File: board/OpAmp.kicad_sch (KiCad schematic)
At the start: 16 parts, among them U4 ${SIM.PARAMS}, U5 ${SIM.PARAMS}, U6 ${SIM.PARAMS}

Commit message: Add OpAmp link
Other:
- note added: "LM358DT"
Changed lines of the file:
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@@
 	(generator_version "9.0")
 	(paper "A4")
+	(text "LM358DT"
+		(exclude_from_sim no)
+		(at 69.088 146.558 0)
+		(effects
+			(font
+				(size 1.27 1.27)
+			)
+			(href "https://www.digikey.com/en/products/detail/stmicroelectronics/LM358DT/591693")
+		)
+	)
 	(junction
 		(at 172.72 133.35)

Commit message: fixed some review issues and footprints
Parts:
- Conn4: footprint (none) -> MRDT_Connectors:MOLEX_SL_04_Vertical
- R10, R11, R12, R13, R14, R15, R4, R5, R6, R7, R8, R9: footprint (none) -> Resistor_SMD:R_0603_1608Metric_Pad0.98x0.95mm_HandSolder
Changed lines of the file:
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@@
 			)
 		)
-		(property "Footprint" ""
+		(property "Footprint" "Resistor_SMD:R_0603_1608Metric_Pad0.98x0.95mm_HandSolder"
 			(at 171.704 139.446 90)
 			(effects
@@
 			)
 		)
-		(property "Footprint" ""
+		(property "Footprint" "Resistor_SMD:R_0603_1608Metric_Pad0.98x0.95mm_HandSolder"
 			(at 122.174 138.176 90)
 			(effects
@@
 			)
 		)
-		(property "Footprint" ""
+		(property "Footprint" "Resistor_SMD:R_0603_1608Metric_Pad0.98x0.95mm_HandSolder"
 			(at 138.684 131.064 90)
 			(effects
@@
 			)
 		)
-		(property "Footprint" ""
+		(property "Footprint" "Resistor_SMD:R_0603_1608Metric_Pad0.98x0.95mm_HandSolder"
 			(at 127.254 138.176 90)
 			(effects
@@
 			)
 		)
-		(property "Footprint" ""
+		(property "Footprint" "Resistor_SMD:R_0603_1608Metric_Pad0.98x0.95mm_HandSolder"
 			(at 225.044 139.446 90)
 			(effects
@@
 			)
 		)
-		(property "Footprint" ""
+		(property "Footprint" "Resistor_SMD:R_0603_1608Metric_Pad0.98x0.95mm_HandSolder"
 			(at 236.474 132.334 90)
 			(effects
@@
 			)
 		)
-		(property "Footprint" ""
+		(property "Footprint" "Resistor_SMD:R_0603_1608Metric_Pad0.98x0.95mm_HandSolder"
 			(at 108.204 117.856 90)
 			(effects
@@
 			)
 		)
-		(property "Footprint" ""
+		(property "Footprint" "Resistor_SMD:R_0603_1608Metric_Pad0.98x0.95mm_HandSolder"
 			(at 176.784 139.446 90)
 			(effects
@@
 			)
 		)
-		(property "Footprint" ""
+		(property "Footprint" "Resistor_SMD:R_0603_1608Metric_Pad0.98x0.95mm_HandSolder"
 			(at 219.964 139.446 90)
 			(effects
@@
 			)
 		)
-		(property "Footprint" ""
+		(property "Footprint" "Resistor_SMD:R_0603_1608Metric_Pad0.98x0.95mm_HandSolder"
 			(at 205.994 119.126 90)
 			(effects
@@
 			)
 		)
-		(property "Footprint" ""
+		(property "Footprint" "MRDT_Connectors:MOLEX_SL_04_Vertical"
 			(at 247.65 76.2 0)
 			(effects
@@
 			)
 		)
-		(property "Footprint" ""
+		(property "Footprint" "Resistor_SMD:R_0603_1608Metric_Pad0.98x0.95mm_HandSolder"
 			(at 157.734 119.126 90)
 			(effects
@@
 			)
 		)
-		(property "Footprint" ""
+		(property "Footprint" "Resistor_SMD:R_0603_1608Metric_Pad0.98x0.95mm_HandSolder"
 			(at 188.214 132.334 90)
 			(effects

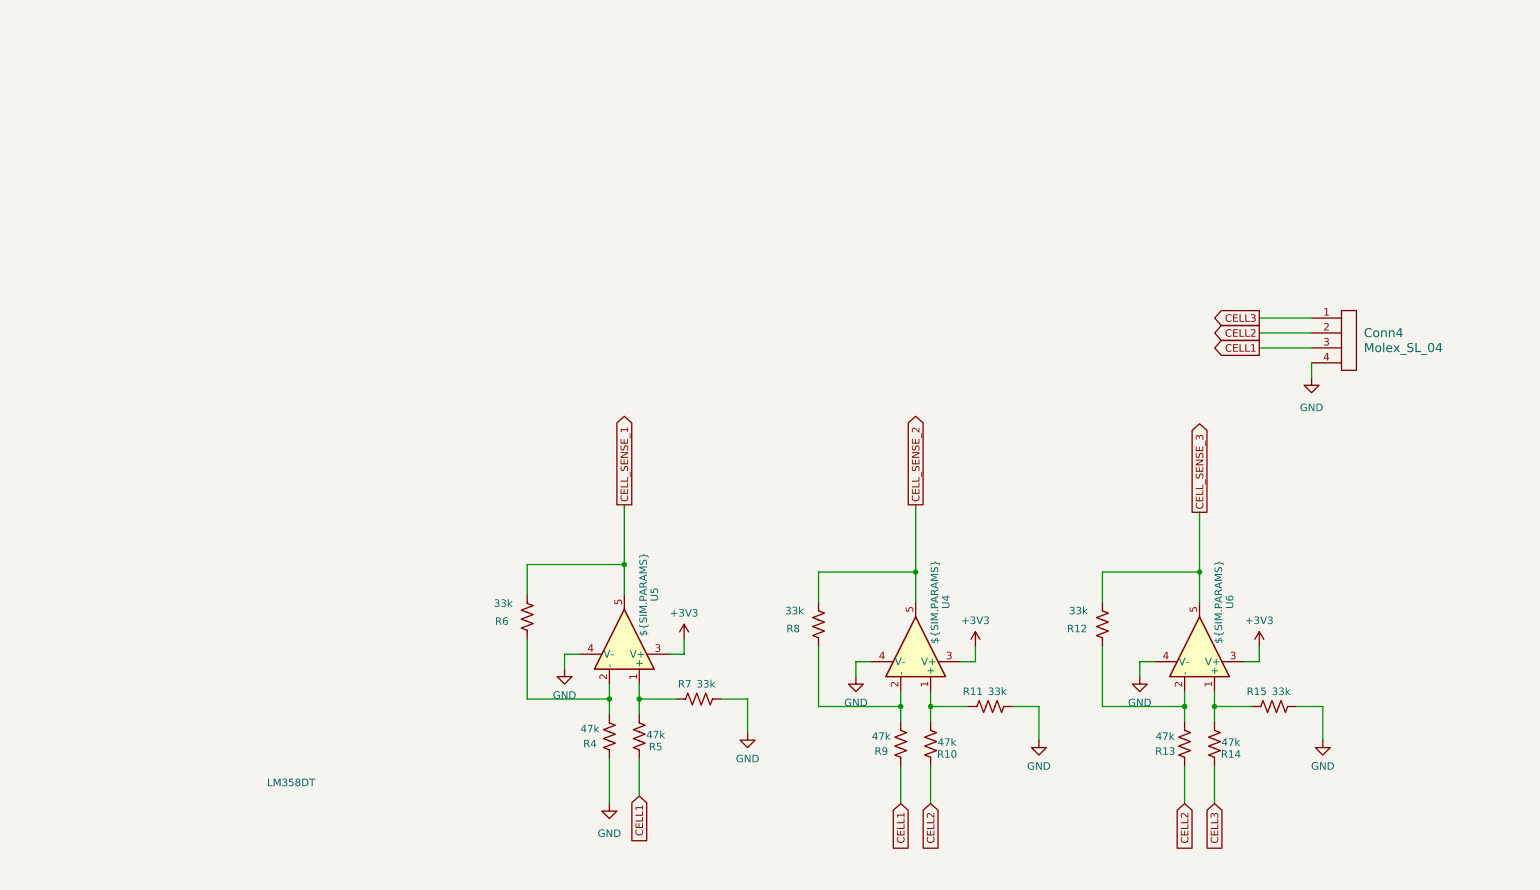
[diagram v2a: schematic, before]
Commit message: Change Gate Driver and Op amp
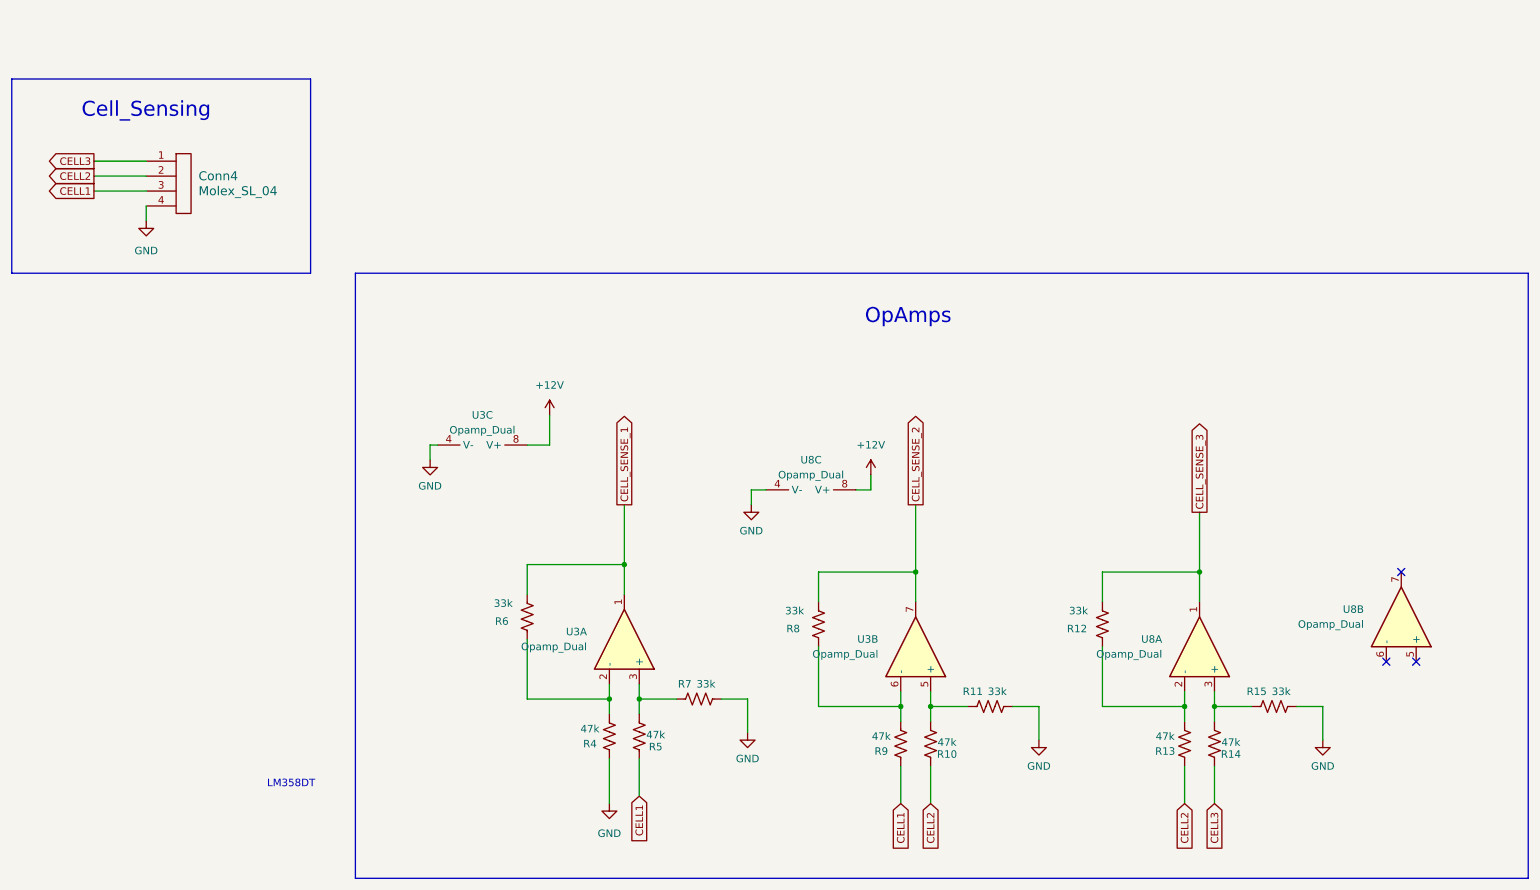
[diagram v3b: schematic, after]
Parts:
- removed U4, U5, U6: ${SIM.PARAMS}, symbol Simulation_SPICE:OPAMP
- added U3, U8: Opamp_Dual, symbol Device:Opamp_Dual
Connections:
- net CELL_SENSE_1: now also U3.1
- net CELL_SENSE_2: now also U3.7
- net CELL_SENSE_3: now also U8.1
- net GND: now also U3.4 (V-), U8.4 (V-)
- net at R8.1, R9.2: now also U3.6 (-)
- net at R4.2, R6.1: now also U3.2 (-)
- net at R5.2, R7.1: now also U3.3 (+)
- net at R14.2, R15.1: now also U8.3 (+)
- net at R10.2, R11.1: now also U3.5 (+)
- net at R12.1, R13.2: now also U8.2 (-)
- new net +12V: U3.8 (V+), U8.8 (V+)
- no-connect marks 0 -> 3
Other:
- note added: "Cell_Sensing"
- note added: "OpAmps"
- moved on the sheet: Conn4

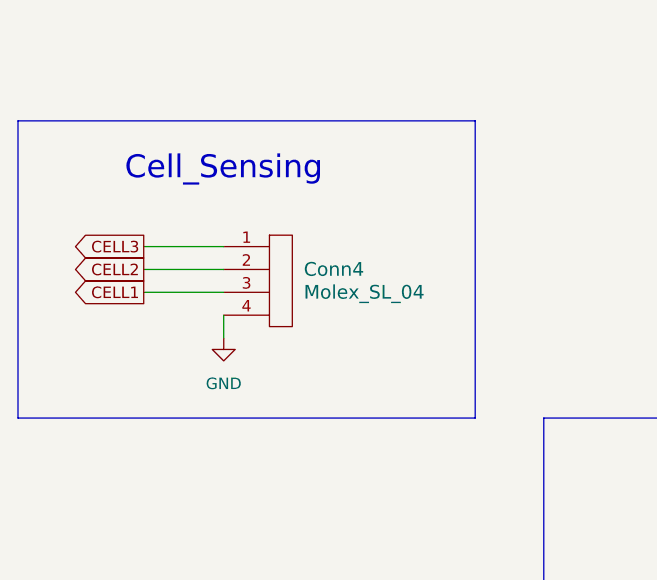
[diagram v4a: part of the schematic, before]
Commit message: fixed tags added buzzer
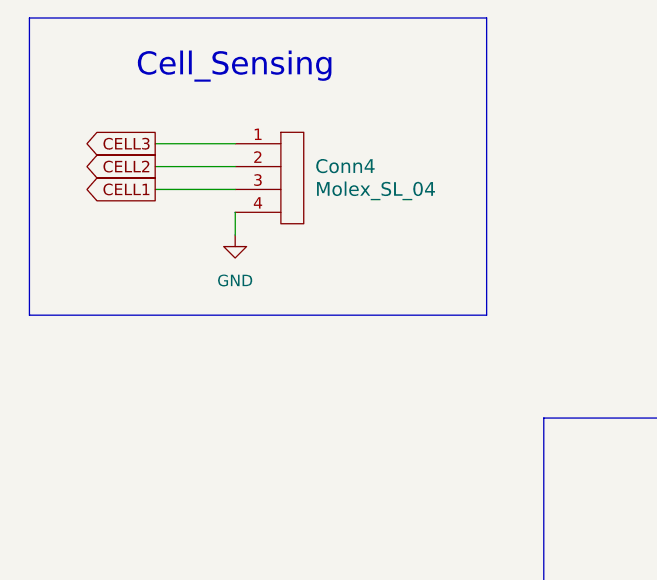
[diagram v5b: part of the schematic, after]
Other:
- moved on the sheet: Conn4
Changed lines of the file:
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@@
 	(paper "A4")
 	(rectangle
-		(start 21.59 26.67)
-		(end 72.39 59.69)
+		(start 22.86 15.24)
+		(end 73.66 48.26)
 		(stroke
 			(width 0)
@@
 	(text "Cell_Sensing"
 		(exclude_from_sim no)
-		(at 44.45 32.004 0)
+		(at 45.72 20.574 0)
 		(effects
 			(font
@@
 	(wire
 		(pts
-			(xy 35.56 40.64) (xy 44.45 40.64)
-		)
-		(stroke
-			(width 0)
-			(type default)
-		)
-	)
-	(wire
-		(pts
-			(xy 35.56 43.18) (xy 44.45 43.18)
+			(xy 36.83 29.21) (xy 45.72 29.21)
+		)
+		(stroke
+			(width 0)
+			(type default)
+		)
+	)
+	(wire
+		(pts
+			(xy 36.83 31.75) (xy 45.72 31.75)
 		)
 		(stroke
@@
 	(wire
 		(pts
-			(xy 35.56 45.72) (xy 44.45 45.72)
+			(xy 36.83 34.29) (xy 45.72 34.29)
 		)
 		(stroke
@@
 	(wire
 		(pts
-			(xy 44.45 50.8) (xy 44.45 48.26)
+			(xy 45.72 39.37) (xy 45.72 36.83)
 		)
 		(stroke
@@
 	(global_label "CELL1"
 		(shape output)
-		(at 35.56 45.72 180)
+		(at 36.83 34.29 180)
 		(fields_autoplaced yes)
 		(effects
@@
 		)
 		(property "Intersheetrefs" "${INTERSHEET_REFS}"
-			(at 26.8901 45.72 0)
+			(at 28.1601 34.29 0)
 			(effects
 				(font
@@
 	(global_label "CELL3"
 		(shape output)
-		(at 35.56 40.64 180)
+		(at 36.83 29.21 180)
 		(fields_autoplaced yes)
 		(effects
@@
 		)
 		(property "Intersheetrefs" "${INTERSHEET_REFS}"
-			(at 26.8901 40.64 0)
+			(at 28.1601 29.21 0)
 			(effects
 				(font
@@
 	(global_label "CELL2"
 		(shape output)
-		(at 35.56 43.18 180)
+		(at 36.83 31.75 180)
 		(fields_autoplaced yes)
 		(effects
@@
 		)
 		(property "Intersheetrefs" "${INTERSHEET_REFS}"
-			(at 26.8901 43.18 0)
+			(at 28.1601 31.75 0)
 			(effects
 				(font
@@
 	(symbol
 		(lib_id "power:GND")
-		(at 44.45 50.8 0)
+		(at 45.72 39.37 0)
 		(unit 1)
 		(exclude_from_sim no)
@@
 		(fields_autoplaced yes)
 		(property "Reference" "#PWR021"
-			(at 44.45 57.15 0)
+			(at 45.72 45.72 0)
 			(effects
 				(font
@@
 		)
 		(property "Value" "GND"
-			(at 44.45 55.88 0)
+			(at 45.72 44.45 0)
 			(effects
 				(font
@@
 		)
 		(property "Footprint" ""
-			(at 44.45 50.8 0)
+			(at 45.72 39.37 0)
 			(effects
 				(font
@@
 		)
 		(property "Datasheet" ""
-			(at 44.45 50.8 0)
+			(at 45.72 39.37 0)
 			(effects
 				(font
@@
 		)
 		(property "Description" "Power symbol creates a global label with name \"GND\" , ground"
-			(at 44.45 50.8 0)
+			(at 45.72 39.37 0)
 			(effects
 				(font
@@
 	(symbol
 		(lib_id "MRDT_Connectors:Molex_SL_04")
-		(at 49.53 49.53 0)
+		(at 50.8 38.1 0)
 		(unit 1)
 		(exclude_from_sim no)
@@
 		(fields_autoplaced yes)
 		(property "Reference" "Conn4"
-			(at 53.34 43.1799 0)
+			(at 54.61 31.7499 0)
 			(effects
 				(font
@@
 		)
 		(property "Value" "Molex_SL_04"
-			(at 53.34 45.7199 0)
+			(at 54.61 34.2899 0)
 			(effects
 				(font
@@
 		)
 		(property "Footprint" "MRDT_Connectors:MOLEX_SL_04_Vertical"
-			(at 49.53 49.53 0)
+			(at 50.8 38.1 0)
 			(effects
 				(font
@@
 		)
 		(property "Datasheet" ""
-			(at 49.53 49.53 0)
+			(at 50.8 38.1 0)
 			(effects
 				(font
@@
 		)
 		(property "Description" ""
-			(at 49.53 49.53 0)
-			(effects
-				(font
+			(at 50.8 38.1 0)
+			(effects
+				(font

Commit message: Add Footprint Assignments
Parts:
- Conn4: footprint MRDT_Connectors:MOLEX_SL_04_Vertical -> MRDT_Connectors:MOLEX_SL_04_Horizontal
- U3, U8: footprint (none) -> Package_SO:SO-8_3.9x4.9mm_P1.27mm
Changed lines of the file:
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@@
 			)
 		)
-		(property "Footprint" ""
+		(property "Footprint" "Package_SO:SO-8_3.9x4.9mm_P1.27mm"
 			(at 101.6 86.36 0)
 			(effects
@@
 			)
 		)
-		(property "Footprint" ""
+		(property "Footprint" "Package_SO:SO-8_3.9x4.9mm_P1.27mm"
 			(at 223.52 123.19 0)
 			(effects
@@
 			)
 		)
-		(property "Footprint" ""
+		(property "Footprint" "Package_SO:SO-8_3.9x4.9mm_P1.27mm"
 			(at 257.81 118.11 0)
 			(effects
@@
 			)
 		)
-		(property "Footprint" "MRDT_Connectors:MOLEX_SL_04_Vertical"
+		(property "Footprint" "MRDT_Connectors:MOLEX_SL_04_Horizontal"
 			(at 50.8 38.1 0)
 			(effects
@@
 			)
 		)
-		(property "Footprint" ""
+		(property "Footprint" "Package_SO:SO-8_3.9x4.9mm_P1.27mm"
 			(at 175.26 123.19 0)
 			(effects
@@
 			)
 		)
-		(property "Footprint" ""
+		(property "Footprint" "Package_SO:SO-8_3.9x4.9mm_P1.27mm"
 			(at 157.48 93.98 0)
 			(effects
@@
 			)
 		)
-		(property "Footprint" ""
+		(property "Footprint" "Package_SO:SO-8_3.9x4.9mm_P1.27mm"
 			(at 125.73 121.92 0)
 			(effects

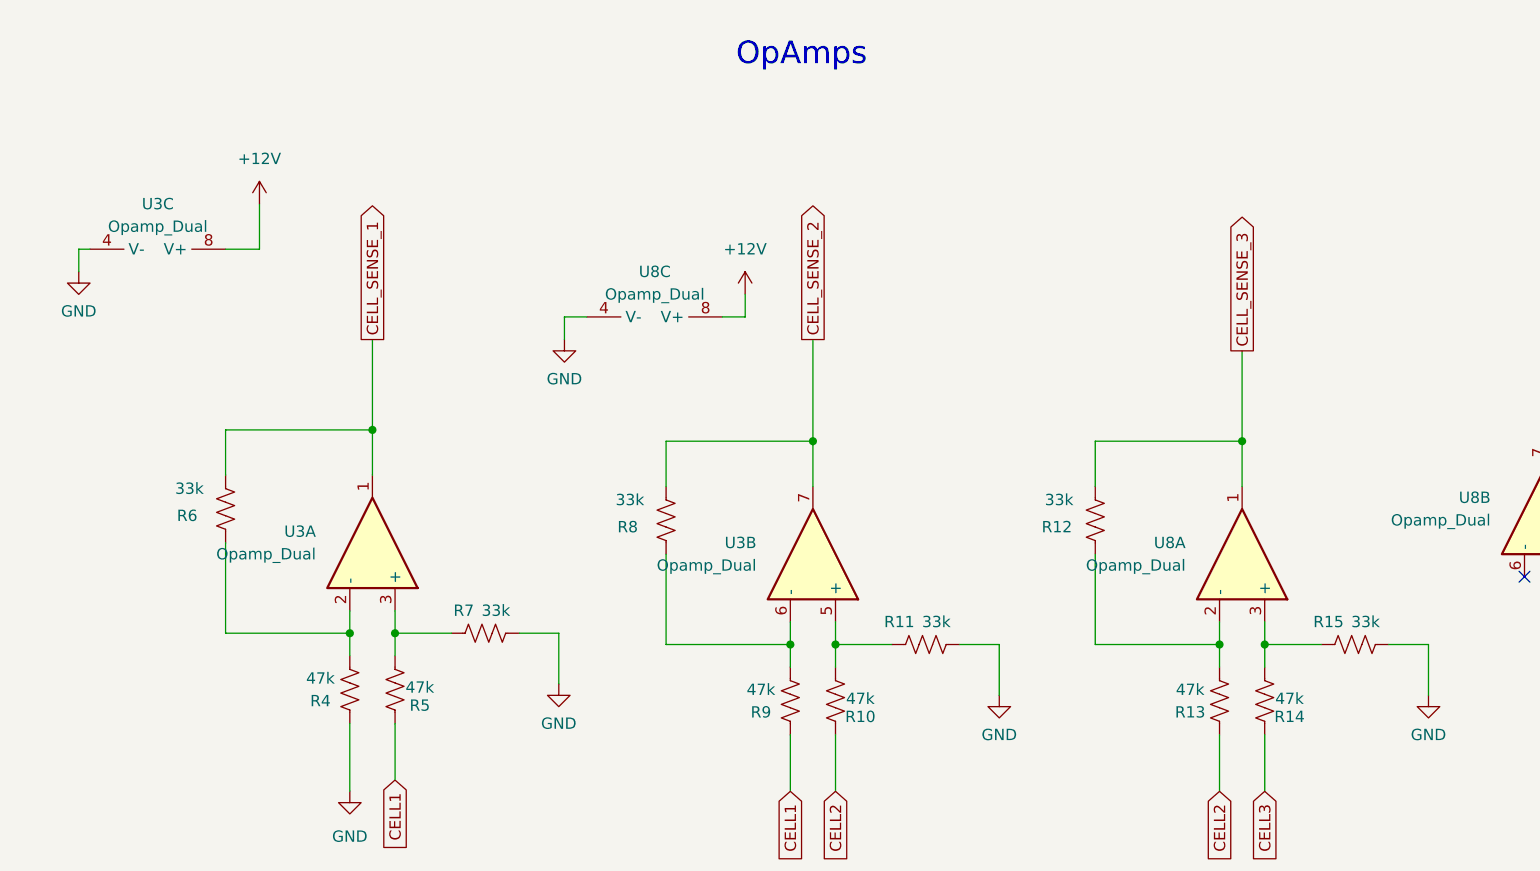
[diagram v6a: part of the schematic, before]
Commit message: Fixed Gain ratio
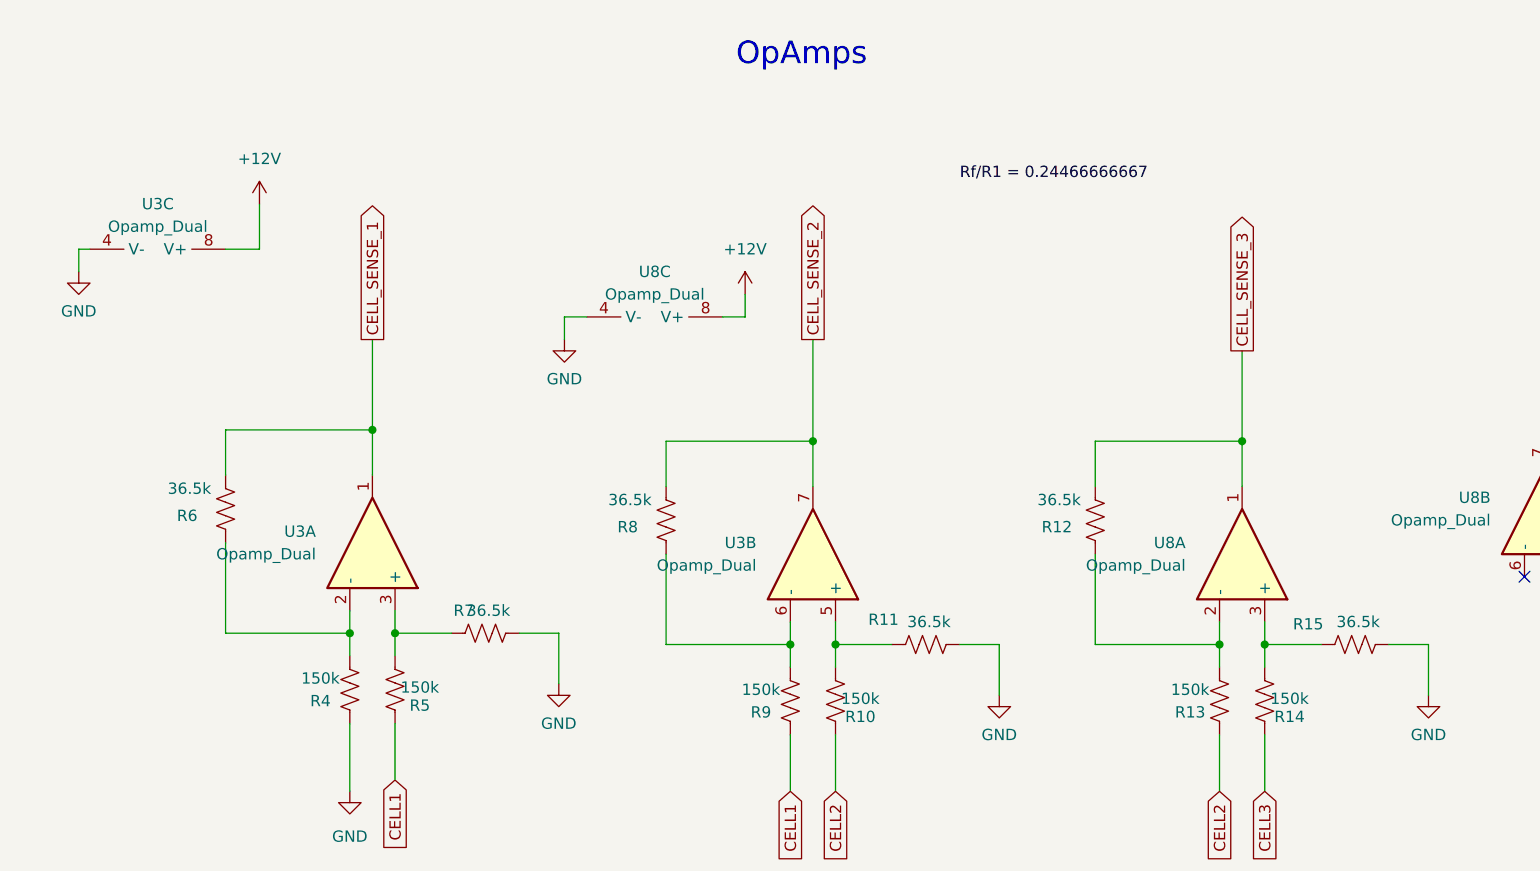
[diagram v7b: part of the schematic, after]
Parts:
- R10, R13, R14, R4, R5, R9: value 47k -> 150k
- R11, R12, R15, R6, R7, R8: value 33k -> 36.5k
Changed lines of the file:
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@@
+		)
+	)
+	(label "Rf{slash}R1 = 0.24466666667"
+		(at 191.77 81.28 0)
+		(effects
+			(font
+				(size 1.27 1.27)
+			)
+			(justify left bottom)
 		)
 	)
@@
 			)
 		)
-		(property "Value" "47k"
+		(property "Value" "150k"
 			(at 169.418 138.43 0)
 			(effects
@@
 			)
 		)
-		(property "Value" "47k"
+		(property "Value" "150k"
 			(at 119.888 137.16 0)
 			(effects
@@
 			)
 		)
-		(property "Value" "33k"
+		(property "Value" "36.5k"
 			(at 141.224 129.54 90)
 			(effects
@@
 			)
 		)
-		(property "Value" "47k"
+		(property "Value" "150k"
 			(at 131.064 138.176 0)
 			(effects
@@
 			)
 		)
-		(property "Value" "47k"
+		(property "Value" "150k"
 			(at 228.854 139.446 0)
 			(effects
@@
 		(dnp no)
 		(property "Reference" "R15"
-			(at 234.9499 130.81 90)
+			(at 232.664 131.064 90)
 			(effects
 				(font
@@
 			)
 		)
-		(property "Value" "33k"
+		(property "Value" "36.5k"
 			(at 239.014 130.81 90)
 			(effects
@@
 			)
 		)
-		(property "Value" "33k"
+		(property "Value" "36.5k"
 			(at 105.156 115.824 0)
 			(effects
@@
 			)
 		)
-		(property "Value" "47k"
+		(property "Value" "150k"
 			(at 180.594 139.446 0)
 			(effects
@@
 			)
 		)
-		(property "Value" "47k"
+		(property "Value" "150k"
 			(at 217.678 138.43 0)
 			(effects
@@
 			)
 		)
-		(property "Value" "33k"
+		(property "Value" "36.5k"
 			(at 202.946 117.094 0)
 			(effects
@@
 			)
 		)
-		(property "Value" "33k"
+		(property "Value" "36.5k"
 			(at 154.686 117.094 0)
 			(effects
@@
 		(dnp no)
 		(property "Reference" "R11"
-			(at 186.6899 130.81 90)
+			(at 184.912 130.556 90)
 			(effects
 				(font
@@
 			)
 		)
-		(property "Value" "33k"
+		(property "Value" "36.5k"
 			(at 190.754 130.81 90)
 			(effects
